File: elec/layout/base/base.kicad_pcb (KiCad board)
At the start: 2 copper layers, 225.7 x 100.8 mm, 0 parts

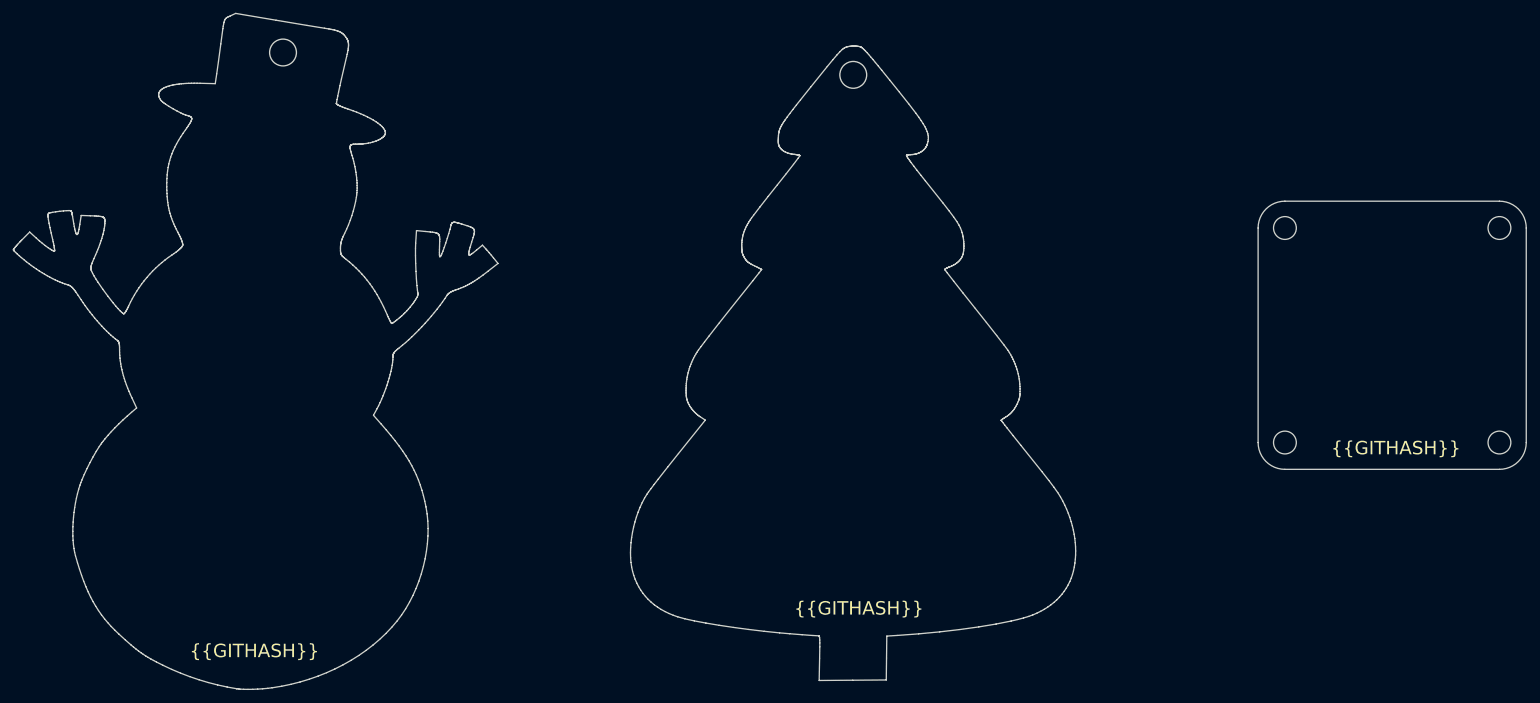
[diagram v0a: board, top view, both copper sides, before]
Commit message: Add layout for base
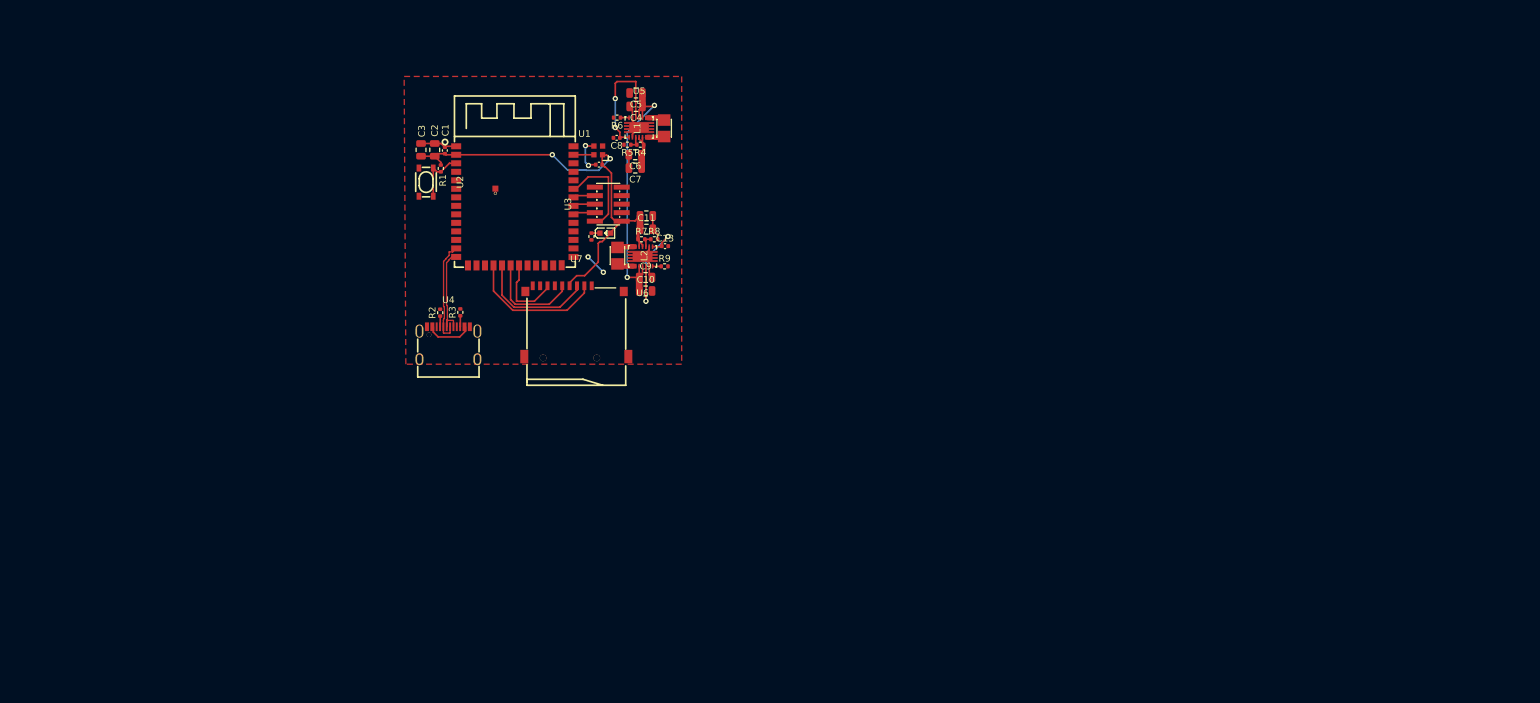
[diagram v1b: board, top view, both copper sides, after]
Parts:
- added C1: 16V 100nF X7R ±10% 0402 Multilayer Ceramic Capacitors MLCC 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, lib:C0402, F.Cu at (100.3, 70.2)
- added C10: 25V 10uF X5R ±10% 0805 Multilayer Ceramic Capacitors MLCC -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, lib:C0805, F.Cu at (130.3, 91.2)
- added C11: 25V 10uF X5R ±10% 0805 Multilayer Ceramic Capacitors MLCC -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, lib:C0805, F.Cu at (130.4, 82.0)
- added C12: 25V 10uF X5R ±10% 0805 Multilayer Ceramic Capacitors MLCC -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, lib:C0805, F.Cu at (130.4, 80.0)
- added C13: 16V 100nF X7R ±10% 0402 Multilayer Ceramic Capacitors MLCC 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, lib:C0402, F.Cu at (133.1, 84.5)
- added C14: 16V 100nF X7R ±10% 0402 Multilayer Ceramic Capacitors MLCC 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, lib:C0402, F.Cu at (123.3, 72.3)
- added C2: 25V 10uF X5R ±10% 0805 Multilayer Ceramic Capacitors MLCC -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, lib:C0805, F.Cu at (98.8, 70.1)
- added C3: 25V 10uF X5R ±10% 0805 Multilayer Ceramic Capacitors MLCC -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, lib:C0805, F.Cu at (96.8, 70.1)
- added C4: 25V 10uF X5R ±10% 0805 Multilayer Ceramic Capacitors MLCC -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, lib:C0805, F.Cu at (128.8, 63.7)
- added C5: 25V 10uF X5R ±10% 0805 Multilayer Ceramic Capacitors MLCC -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, lib:C0805, F.Cu at (128.8, 61.7)
- added C6: 25V 10uF X5R ±10% 0805 Multilayer Ceramic Capacitors MLCC -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, lib:C0805, F.Cu at (128.7, 70.9)
- added C7: 25V 10uF X5R ±10% 0805 Multilayer Ceramic Capacitors MLCC -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, lib:C0805, F.Cu at (128.7, 72.9)
- added C8: 16V 100nF X7R ±10% 0402 Multilayer Ceramic Capacitors MLCC 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, lib:C0402, F.Cu at (125.9, 68.3)
- added C9: 25V 10uF X5R ±10% 0805 Multilayer Ceramic Capacitors MLCC -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, lib:C0805, F.Cu at (130.3, 89.2)
- added L1: ?, lib:IND-SMD_L2.5-W2.0_WPN252012H, F.Cu at (133.0, 66.9)
- added L2: ?, lib:IND-SMD_L2.5-W2.0_WPN252012H, F.Cu at (126.1, 85.9)
- added LED1: ?, lib:LED0603-RD, F.Cu at (124.2, 82.5)
- added R1: 62.5mW Thick Film Resistors 50V ±100ppm/℃ ±1% 10kΩ 0402 Chi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, lib:R0402, F.Cu at (99.7, 72.9)
- added R10: 62.5mW Thick Film Resistors 50V ±100ppm/℃ ±1% 330Ω 0402 Chi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, lib:R0402, F.Cu at (122.2, 83.1)
- added R2: 62.5mW Thick Film Resistors 50V ±100ppm/℃ ±1% 4.7kΩ 0402 Ch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, lib:R0402, F.Cu at (99.6, 94.4)
- added R3: 62.5mW Thick Film Resistors 50V ±100ppm/℃ ±1% 4.7kΩ 0402 Ch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, lib:R0402, F.Cu at (102.6, 94.4)
- added R4: 62.5mW 50V ±100ppm/℃ ±1% 25.5kΩ 0402 Chip Resistor - Surfac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, lib:R0402, F.Cu at (129.5, 69.4)
- added R5: 62.5mW Thick Film Resistors 50V ±1% ±200ppm/℃ 2.8kΩ 0402 Ch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, lib:R0402, F.Cu at (127.5, 69.4)
- added R6: 62.5mW Thick Film Resistors 50V ±100ppm/℃ ±1% 1MΩ 0402 Chip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, lib:R0402, F.Cu at (126.0, 65.3)
- added R7: 62.5mW Thick Film Resistors 50V ±100ppm/℃ ±1% 23.7kΩ 0402 C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, lib:R0402, F.Cu at (129.6, 83.5)
- added R8: 62.5mW Thick Film Resistors 50V ±100ppm/℃ ±1% 4.3kΩ 0402 Ch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, lib:R0402, F.Cu at (131.5, 83.5)
- added R9: 62.5mW Thick Film Resistors 50V ±100ppm/℃ ±1% 1MΩ 0402 Chip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, lib:R0402, F.Cu at (133.1, 87.5)
- added U1: ?, lib:WIRELM-SMD_ESP32-S3-WROOM-1, F.Cu at (110.7, 78.5)
- added U2: ?, lib:KEY-SMD_4P-L4.2-W3.2-P2.20-LS4.6, F.Cu at (97.5, 74.9)
- added U3: ?, lib:HDR-SMD_10P-P1.27-V-M-R2-C5-LS5.3, F.Cu at (124.7, 78.2)
- added U4: ?, lib:USB-C-SMD_KH-TYPE-C-16P, F.Cu at (100.8, 98.9)
- added U5: ?, lib:VSON-14_L4.0-W3.0-P0.50-BL-EP_TI_DSJ, F.Cu at (129.3, 66.8)
- added U6: ?, lib:VSON-14_L4.0-W3.0-P0.50-BL-EP_TI_DSJ, F.Cu at (129.8, 86.0)
- added U7: ?, lib:TF-SMD_TF-01A, F.Cu at (119.9, 95.7)
- added U8: ?, lib:LED-SMD_4P-L2.0-W2.0-BR, F.Cu at (123.2, 70.2)
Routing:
- net uc.ic-vcc: track 0.00 -> 68.0 mm, vias 0 -> 2
- net vcc: track 0.00 -> 42.3 mm, vias 0 -> 2
- net uc.ic-gnd: track 0.00 -> 31.3 mm, vias 0 -> 4
- net cs: track 0.00 -> 20.7 mm
- net _3v3_reg.ic-vina: track 0.00 -> 19.5 mm, vias 0 -> 2
- net _5v_reg.ic-vina: track 0.00 -> 18.4 mm, vias 0 -> 2
- net mosi: track 0.00 -> 18.1 mm
- net usb-: track 0.00 -> 15.7 mm
- net sck: track 0.00 -> 14.7 mm
- net usb+: track 0.00 -> 14.3 mm
- net tms: track 0.00 -> 14.0 mm
- net miso: track 0.00 -> 11.3 mm
- net en: track 0.00 -> 8.40 mm
- net usb_conn-vcc: track 0.00 -> 6.90 mm
- net _5v_reg-vcc: track 0.00 -> 6.20 mm
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- added copper zone on F.Cu, net uc.ic-gnd
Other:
- board outline removed
- board text removed: "{{GITHASH}}"
